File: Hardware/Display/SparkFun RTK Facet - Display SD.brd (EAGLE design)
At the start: 49.5 x 22 mm, 48 parts, among them J1 FPC_12_0.5MM_BACKFLIP, J2 MICRO-SD-PUSH-PUSH-EXT-PIN, U13 LIS2DH12

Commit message: Remove silk from around the accel FP for DFM.
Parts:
- JP3: value (none) -> JUMPER-SMT_2_NO_SILK
- U13: value LIS2DH12 -> LIS2DH12NS; device SparkFun-Sensors:LGA-12-LISDH12 -> SparkFun-Sensors:LGA-12-LISDH12-NOSILK
- moved U$11 12.0 mm to (20.7, 14.5)
- moved U$10 12.0 mm to (18.1, 11.8)
- moved U$12 12.0 mm to (16.6, 14.4)
- moved U$9 5.59 mm to (11.0, 19.2), turned to 90 degrees
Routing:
- net N$4: track 0.00 -> 1.22 mm
- net N$5: track 0.00 -> 0.89 mm
- net GND: vias 21 -> 22
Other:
- board text added: "v17"
- board text removed: "v16"
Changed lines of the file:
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@@
 <setting verticaltext="up"/>
 </settings>
-<grid distance="0.05" unitdist="inch" unit="inch" style="lines" multiple="1" display="yes" altdistance="0.005" altunitdist="inch" altunit="inch"/>
+<grid distance="1" unitdist="mm" unit="mm" style="lines" multiple="1" display="yes" altdistance="0.1" altunitdist="mm" altunit="mm"/>
 <layers>
 <layer number="1" name="Top/Vert" color="4" fill="1" visible="yes" active="yes"/>
@@
 <board>
 <plain>
-<text x="3.75" y="1" size="1.016" layer="1" font="vector" ratio="20" rot="R180" align="center">v16</text>
+<text x="3.75" y="1" size="1.016" layer="1" font="vector" ratio="20" rot="R180" align="center">v17</text>
 <wire x1="0" y1="0" x2="0" y2="22" width="0.05" layer="20"/>
 <wire x1="49.5" y1="22" x2="49.5" y2="0" width="0.05" layer="20"/>
@@
 <wire x1="19.75" y1="21" x2="19.75" y2="22" width="0.05" layer="20"/>
 <wire x1="29.75" y1="21" x2="19.75" y2="21" width="0.05" layer="20"/>
-<wire x1="6.766" y1="10.698" x2="6.766" y2="8.758" width="0.2032" layer="21"/>
-<wire x1="6.766" y1="8.758" x2="6.258" y2="9.266" width="0.2032" layer="21"/>
-<wire x1="6.766" y1="8.758" x2="7.274" y2="9.266" width="0.2032" layer="21"/>
-<circle x="6.766" y="10.571" radius="0.803215625" width="0.2032" layer="21"/>
-<circle x="6.766" y="10.571" radius="0.127" width="0.508" layer="21"/>
-<wire x1="6.766" y1="10.598" x2="8.606" y2="10.598" width="0.2032" layer="21" curve="-0.360962"/>
-<wire x1="8.606" y1="10.598" x2="8.098" y2="10.09" width="0.2032" layer="21"/>
-<wire x1="8.606" y1="10.598" x2="8.098" y2="11.106" width="0.2032" layer="21"/>
+<wire x1="18.196" y1="14.508" x2="18.196" y2="12.568" width="0.2032" layer="21"/>
+<wire x1="18.196" y1="12.568" x2="17.688" y2="13.076" width="0.2032" layer="21"/>
+<wire x1="18.196" y1="12.568" x2="18.704" y2="13.076" width="0.2032" layer="21"/>
+<circle x="18.196" y="14.381" radius="0.803215625" width="0.2032" layer="21"/>
+<circle x="18.196" y="14.381" radius="0.127" width="0.508" layer="21"/>
+<wire x1="18.196" y1="14.408" x2="20.036" y2="14.408" width="0.2032" layer="21" curve="-0.360962"/>
+<wire x1="20.036" y1="14.408" x2="19.528" y2="13.9" width="0.2032" layer="21"/>
+<wire x1="20.036" y1="14.408" x2="19.528" y2="14.916" width="0.2032" layer="21"/>
 <dimension x1="0" y1="22" x2="0" y2="0" x3="-4" y3="11" textsize="1" layer="47" width="0.1"/>
 <dimension x1="0" y1="22" x2="49.5" y2="22" x3="24.75" y3="26" textsize="1" layer="47" width="0.1"/>
@@
 <attribute name="VALUE" x="16.488" y="18" size="0.6096" layer="27" font="vector" ratio="20" rot="R270" align="top-center"/>
 </element>
-<element name="JP3" library="SparkFun-Jumpers" package="SMT-JUMPER_2_NO_SILK" package3d_urn="urn:adsk.eagle:package:39279/1" value="" x="25.25" y="5" smashed="yes" rot="MR90">
+<element name="JP3" library="SparkFun-Jumpers" package="SMT-JUMPER_2_NO_SILK" package3d_urn="urn:adsk.eagle:package:39279/1" value="JUMPER-SMT_2_NO_SILK" x="25.25" y="5" smashed="yes" rot="MR90">
 <attribute name="NAME" x="26.393" y="5" size="0.6096" layer="26" font="vector" ratio="20" rot="MR90" align="bottom-center"/>
 <attribute name="VALUE" x="24.107" y="5" size="0.6096" layer="28" font="vector" ratio="20" rot="MR90" align="top-center"/>
@@
 </element>
 <element name="U$1" library="output" package="SD#DIS0" value="" x="33.75" y="16.3" smashed="yes"/>
-<element name="U13" library="SparkFun-Sensors" package="LGA-12-LISDH12" value="LIS2DH12" x="6.75" y="13" smashed="yes">
-<attribute name="DIGIKEY" value="497-14851-2-ND" x="1.75" y="18" size="1.778" layer="27" font="vector" ratio="15" display="off"/>
+<element name="U13" library="SparkFun-Sensors" package="LGA-12-LISDH12-NOSILK" value="LIS2DH12NS" x="6.75" y="13" smashed="yes">
 <attribute name="NAME" x="6.75" y="14.2192" size="0.6096" layer="25" font="vector" ratio="20" align="bottom-center"/>
 <attribute name="PROD_ID" value="IC-14229" x="1.75" y="18" size="1.778" layer="27" font="vector" ratio="15" display="off"/>
@@
 </element>
 <element name="U$2" library="output" package="OVERLAY0" value="" x="24.75" y="9.88" smashed="yes"/>
-<element name="U$9" library="output" package="POWER0" value="" x="6.75" y="15.6" smashed="yes"/>
-<element name="U$10" library="output" package="X0" value="" x="6.65" y="8" smashed="yes" rot="R180"/>
-<element name="U$11" library="output" package="Y1" value="" x="9.25" y="10.7" smashed="yes"/>
-<element name="U$12" library="output" package="Z2" value="" x="5.15" y="10.6" smashed="yes" rot="R180"/>
+<element name="U$9" library="output" package="POWER0" value="" x="11.049" y="19.177" smashed="yes" rot="R90"/>
+<element name="U$10" library="output" package="X0" value="" x="18.08" y="11.81" smashed="yes" rot="R180"/>
+<element name="U$11" library="output" package="Y1" value="" x="20.68" y="14.51" smashed="yes"/>
+<element name="U$12" library="output" package="Z2" value="" x="16.58" y="14.41" smashed="yes" rot="R180"/>
 <element name="U$13" library="output" package="RTK_FACET0" value="" x="8.255" y="2.413" smashed="yes"/>
 <element name="U$5" library="output" package="RTK5#SVG0" value="" x="13.25" y="15" smashed="yes"/>
@@
 <contactref element="J3" pad="1"/>
 <via x="8.346" y="8.92" extent="1-16" drill="0.381"/>
+<via x="29.694" y="13.789" extent="1-16" drill="0.381"/>
 </signal>
 <signal name="VCOMH">
@@
 <wire x1="27.25" y1="11.25" x2="27.5" y2="11.5" width="0.1778" layer="1"/>
 </signal>
+<signal name="N$4">
+<wire x1="7.62" y1="14.5288" x2="8.2804" y2="14.5288" width="0.1778" layer="1"/>
+<wire x1="8.2804" y1="14.5288" x2="8.2804" y2="13.97" width="0.1778" layer="1"/>
+</signal>
+<signal name="N$5">
+<wire x1="5.5372" y1="11.4808" x2="5.2324" y2="11.4808" width="0.1778" layer="1"/>
+<wire x1="5.2324" y1="11.4808" x2="5.2324" y2="12.065" width="0.1778" layer="1"/>
+</signal>
 </signals>

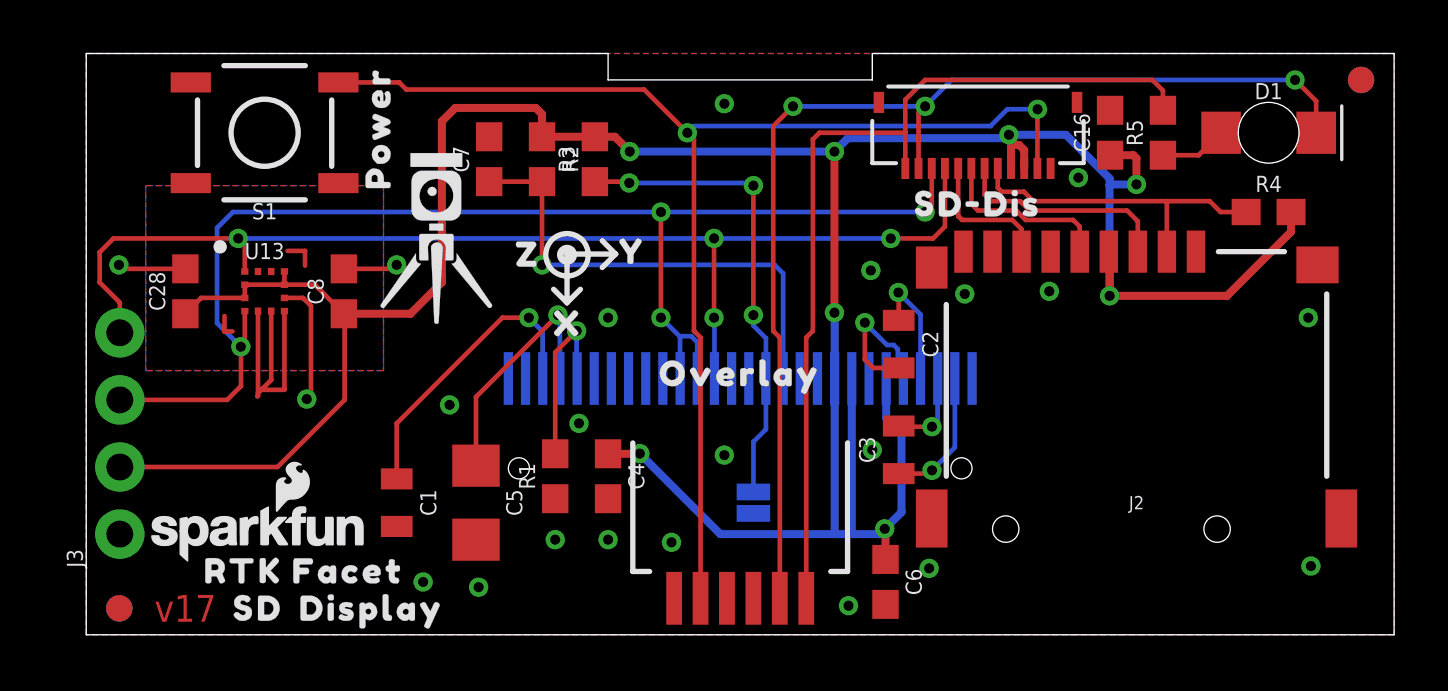
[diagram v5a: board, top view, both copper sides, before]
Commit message: Convert connector and display boards to KiCad
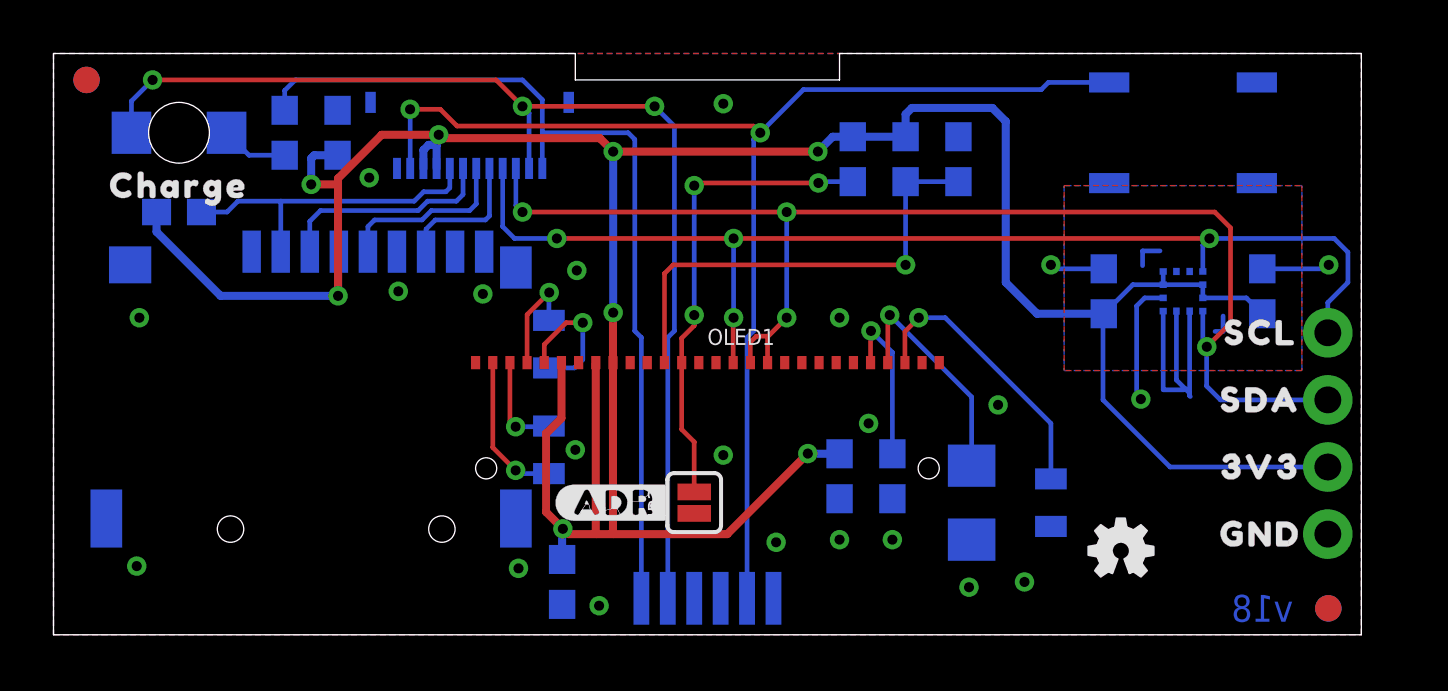
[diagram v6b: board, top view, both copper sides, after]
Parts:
- OLED1: value OLED0.66 -> OLED0.66-TRIMTRIM; device SparkFun-Displays:OLED-0.66-64X48 -> SparkFun-Displays:OLED-0.66-64X48-TRIM
- moved FRAME1 100.6 mm to (-26.2, -12.5), flipped to the bottom
- moved U$6 79.2 mm to (-15.5, 50.6), flipped to the bottom
- moved FID2 48.2 mm to (0.01, 21.0), flipped to the top
- moved FID3 48.2 mm to (0.01, 21.0), flipped to the bottom
- moved FID1 45.8 mm to (47.0, 1.00), flipped to the top
- moved FID4 45.8 mm to (47.0, 1.00), flipped to the bottom
- moved J3 45.7 mm to (47.0, 3.81), flipped to the bottom
- moved D1 41.2 mm to (3.51, 19.0), flipped to the bottom
- moved R4 41.2 mm to (3.51, 16.0), flipped to the bottom
- moved U$8 41.2 mm to (3.51, 17.0), flipped to the top
- moved C28 40.8 mm to (44.5, 13.0), flipped to the bottom
- moved U$14 40.6 mm to (44.5, 6.35), flipped to the top
- moved U$15 40.6 mm to (44.5, 3.81), flipped to the top
- moved U$16 40.6 mm to (44.5, 11.4), flipped to the top
- moved U$17 40.6 mm to (44.5, 8.89), flipped to the top
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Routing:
- net 3.3V: track 118.4 -> 119.6 mm
- net ESP_21/SDA: track 50.1 -> 48.9 mm
- net VCOMH: track 9.42 -> 8.82 mm
- net C1P: track 4.66 -> 4.06 mm
- net VCC: track 11.3 -> 10.7 mm
- net N$1: track 5.15 -> 5.75 mm
- net RESET: track 18.4 -> 17.8 mm
- net C2N: track 3.18 -> 3.78 mm
- net IREF: track 6.79 -> 6.19 mm
- net ESP_22/SCL: track 44.6 -> 44.0 mm
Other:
- board text added: "v18"
- board text removed: "v17"
